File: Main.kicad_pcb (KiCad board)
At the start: 2 copper layers, 99.1 x 78.7 mm, 45 parts, among them J1 Conn_01x01_Female, J10 Conn_01x01_Female, J11 Conn_01x01_Female, J12 Conn_01x01_Female, J2 Conn_01x01_Female, J3 Conn_01x01_Female, J4 Conn_01x02_Female, J5 Conn_01x01_Female, J6 Conn_01x03, J7 Conn_01x03, J8 Conn_01x06, J9 Conn_01x01_Female, Q1 CSD17307Q5A, Q2 CSD17307Q5A, SW1 SW_Push, SW2 SW_Push, SW3 SW_Push, SW4 SW_Push, U1 LTC4002ES8-4.2, U2 SI6423, U3 LTC6995-1, U4 TPS2557

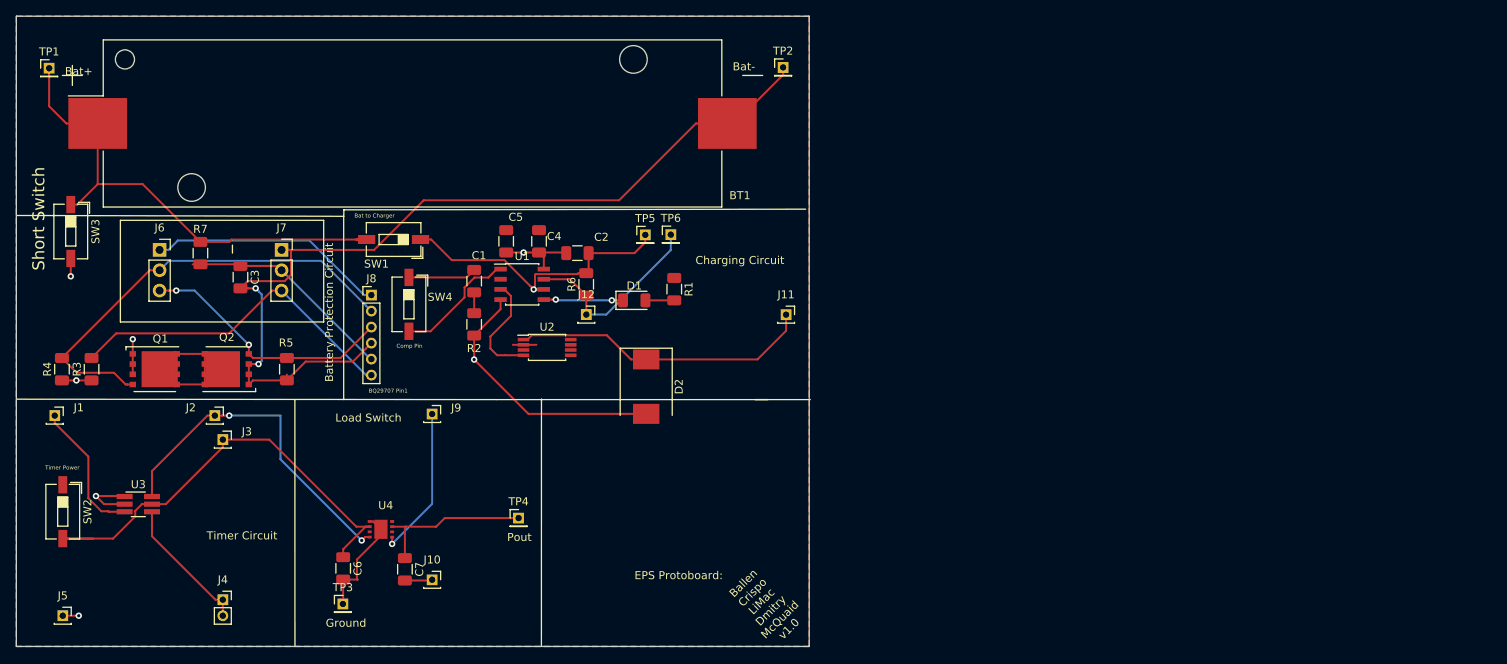
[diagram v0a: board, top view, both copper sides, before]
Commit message: changed_resistor
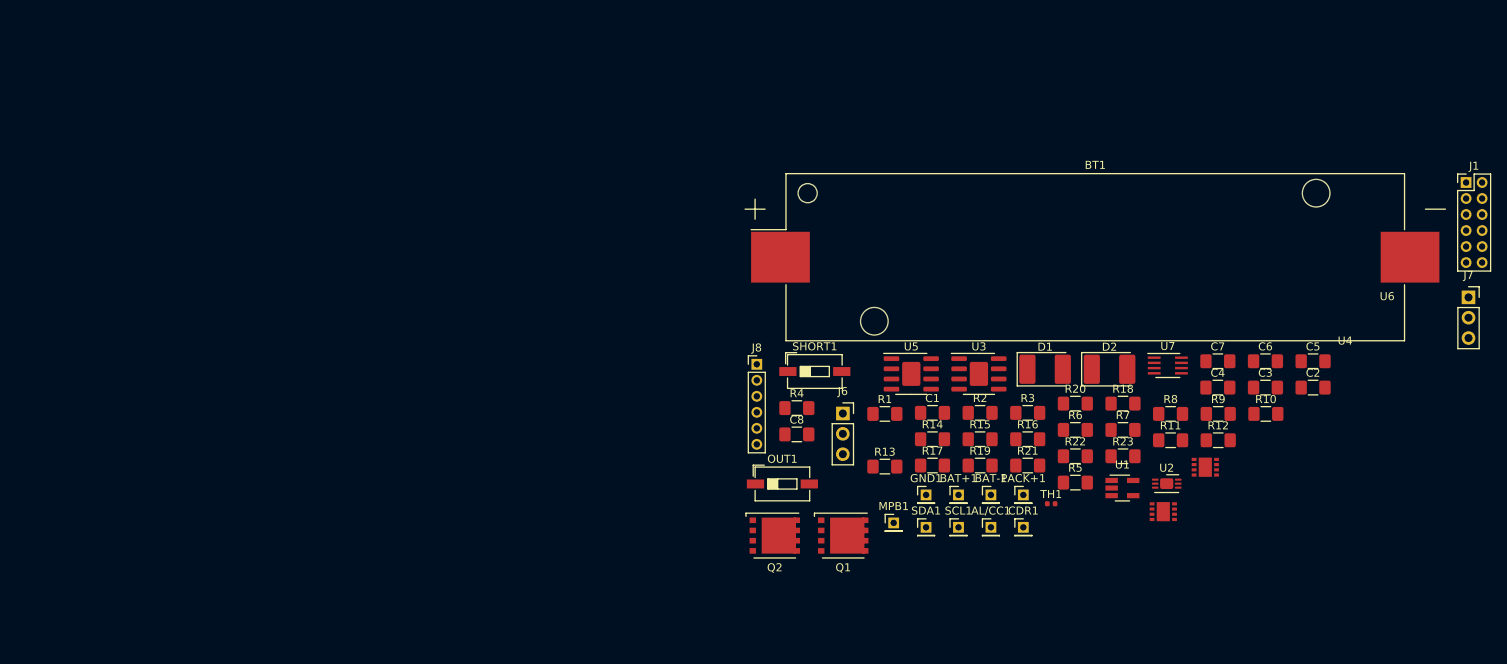
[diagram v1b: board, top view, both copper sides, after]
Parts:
- removed J10, J11, J12, J2, J3, J5, J9: Conn_01x01_Female, Connector_PinSocket_2.00mm:PinSocket_1x01_P2.00mm_Vertical
- removed J4: Conn_01x02_Female, Connector_PinSocket_2.00mm:PinSocket_1x02_P2.00mm_Vertical
- removed SW1, SW2, SW3, SW4: SW_Push, Button_Switch_SMD:SW_DIP_SPSTx01_Slide_6.7x4.1mm_W6.73mm_P2.54mm_LowProfile_JPin
- removed TP1, TP2, TP3, TP4, TP5, TP6: TestPoint, Connector_PinHeader_2.00mm:PinHeader_1x01_P2.00mm_Vertical
- added AL/CC1: TestPoint, Connector_PinHeader_2.00mm:PinHeader_1x01_P2.00mm_Vertical, F.Cu at (145.6, 86.8)
- added BAT+1: TestPoint, Connector_PinHeader_2.00mm:PinHeader_1x01_P2.00mm_Vertical, F.Cu at (141.5, 82.7)
- added BAT-1: TestPoint, Connector_PinHeader_2.00mm:PinHeader_1x01_P2.00mm_Vertical, F.Cu at (145.6, 82.7)
- added C8: 0.1u, Capacitor_SMD:C_1206_3216Metric_Pad1.42x1.75mm_HandSolder, F.Cu at (121.3, 75.2)
- added CDR1: TestPoint, Connector_PinHeader_2.00mm:PinHeader_1x01_P2.00mm_Vertical, F.Cu at (149.6, 86.8)
- added GND1: TestPoint, Connector_PinHeader_2.00mm:PinHeader_1x01_P2.00mm_Vertical, F.Cu at (137.5, 82.7)
- added MPB1: TestPoint, Connector_PinHeader_2.00mm:PinHeader_1x01_P2.00mm_Vertical, F.Cu at (133.4, 86.2)
- added OUT1: SW_Push, Button_Switch_SMD:SW_DIP_SPSTx01_Slide_6.7x4.1mm_W6.73mm_P2.54mm_LowProfile_JPin, F.Cu at (119.5, 81.3)
- added PACK+1: TestPoint, Connector_PinHeader_2.00mm:PinHeader_1x01_P2.00mm_Vertical, F.Cu at (149.6, 82.7)
- added R10: 332k, Resistor_SMD:R_1206_3216Metric_Pad1.42x1.75mm_HandSolder, F.Cu at (179.9, 72.6)
- added R11: 167k, Resistor_SMD:R_1206_3216Metric_Pad1.42x1.75mm_HandSolder, F.Cu at (168.0, 75.9)
- added R12: 1.64M, Resistor_SMD:R_1206_3216Metric_Pad1.42x1.75mm_HandSolder, F.Cu at (174.0, 75.9)
- added R13: 374k, Resistor_SMD:R_1206_3216Metric_Pad1.42x1.75mm_HandSolder, F.Cu at (132.3, 79.2)
- added R14: 1.43M, Resistor_SMD:R_1206_3216Metric_Pad1.42x1.75mm_HandSolder, F.Cu at (138.3, 75.8)
- added R15: 562k, Resistor_SMD:R_1206_3216Metric_Pad1.42x1.75mm_HandSolder, F.Cu at (144.2, 75.8)
- added R16: 14.7m, Resistor_SMD:R_1206_3216Metric_Pad1.42x1.75mm_HandSolder, F.Cu at (150.2, 75.8)
- added R17: 56.2k, Resistor_SMD:R_1206_3216Metric_Pad1.42x1.75mm_HandSolder, F.Cu at (138.3, 79.0)
- added R18: 100k, Resistor_SMD:R_1206_3216Metric_Pad1.42x1.75mm_HandSolder, F.Cu at (162.1, 71.3)
- added R19: 66.5k, Resistor_SMD:R_1206_3216Metric_Pad1.42x1.75mm_HandSolder, F.Cu at (144.2, 79.0)
- added R20: 29.4k, Resistor_SMD:R_1206_3216Metric_Pad1.42x1.75mm_HandSolder, F.Cu at (156.1, 71.3)
- added R21: 59.0k, Resistor_SMD:R_1206_3216Metric_Pad1.42x1.75mm_HandSolder, F.Cu at (150.2, 79.0)
- added R22: 66.5k, Resistor_SMD:R_1206_3216Metric_Pad1.42x1.75mm_HandSolder, F.Cu at (156.1, 77.9)
- added R23: 100k, Resistor_SMD:R_1206_3216Metric_Pad1.42x1.75mm_HandSolder, F.Cu at (162.1, 77.9)
- added R8: 898k, Resistor_SMD:R_1206_3216Metric_Pad1.42x1.75mm_HandSolder, F.Cu at (168.0, 72.6)
- added R9: 28k, Resistor_SMD:R_1206_3216Metric_Pad1.42x1.75mm_HandSolder, F.Cu at (174.0, 72.6)
- added SCL1: TestPoint, Connector_PinHeader_2.00mm:PinHeader_1x01_P2.00mm_Vertical, F.Cu at (141.5, 86.8)
- added SDA1: TestPoint, Connector_PinHeader_2.00mm:PinHeader_1x01_P2.00mm_Vertical, F.Cu at (137.5, 86.8)
- added SHORT1: SW_Push, Button_Switch_SMD:SW_DIP_SPSTx01_Slide_6.7x4.1mm_W6.73mm_P2.54mm_LowProfile_JPin, F.Cu at (123.6, 67.3)
- added TH1: TDK10k, Resistor_SMD:R_0402_1005Metric, F.Cu at (153.1, 83.8)
- added U5: LM393, Package_SO:SOIC-8-1EP_3.9x4.9mm_P1.27mm_EP2.29x3mm, F.Cu at (135.6, 67.6)
- added U6: TPS2557, tps2557:TPS2557, F.Cu at (171.0, 78.3)
- added U7: SN74LVC2G08, Package_SO:SSOP-8_2.95x2.8mm_P0.65mm, F.Cu at (167.7, 66.5)
- C1: value 0.47u -> 0.022uF; footprint Capacitor_SMD:C_1206_3216Metric -> Capacitor_SMD:C_1206_3216Metric_Pad1.42x1.75mm_HandSolder
- C2: value 22u -> 0.1u; footprint Capacitor_SMD:C_1206_3216Metric -> Capacitor_SMD:C_1206_3216Metric_Pad1.42x1.75mm_HandSolder
- C3: footprint Capacitor_SMD:C_1206_3216Metric -> Capacitor_SMD:C_1206_3216Metric_Pad1.42x1.75mm_HandSolder
- C4: value 10u -> 0.1u; footprint Capacitor_SMD:C_1206_3216Metric -> Capacitor_SMD:C_1206_3216Metric_Pad1.42x1.75mm_HandSolder
- C5: value 0.1u -> 0.22u; footprint Capacitor_SMD:C_1206_3216Metric -> Capacitor_SMD:C_1206_3216Metric_Pad1.42x1.75mm_HandSolder
- C6: value 0.1u -> 10u; footprint Capacitor_SMD:C_1206_3216Metric -> Capacitor_SMD:C_1206_3216Metric_Pad1.42x1.75mm_HandSolder
- C7: value 150u -> 0.22u; footprint Capacitor_SMD:C_1206_3216Metric -> Capacitor_SMD:C_1206_3216Metric_Pad1.42x1.75mm_HandSolder
- D1: value LED -> D_Schottky; footprint LED_SMD:LED_1206_3216Metric -> Diode_SMD:D_2114_3652Metric_Castellated
- D2: value B330 -> D_Schottky; footprint Diode_SMD:D_SMC -> Diode_SMD:D_2114_3652Metric_Castellated
- J1: value Conn_01x01_Female -> Conn_02x06_Top_Bottom; footprint Connector_PinSocket_2.00mm:PinSocket_1x01_P2.00mm_Vertical -> Connector_PinHeader_2.00mm:PinHeader_2x06_P2.00mm_Vertical
- R1: value 2k -> 898k; footprint Resistor_SMD:R_1206_3216Metric -> Resistor_SMD:R_1206_3216Metric_Pad1.42x1.75mm_HandSolder
- R2: value 2.2k -> 898k; footprint Resistor_SMD:R_1206_3216Metric -> Resistor_SMD:R_1206_3216Metric_Pad1.42x1.75mm_HandSolder
- R3, R4, R5, R7: footprint Resistor_SMD:R_1206_3216Metric -> Resistor_SMD:R_1206_3216Metric_Pad1.42x1.75mm_HandSolder
- R6: value 59m -> 6k; footprint Resistor_SMD:R_1206_3216Metric -> Resistor_SMD:R_1206_3216Metric_Pad1.42x1.75mm_HandSolder
- U1: value LTC4002ES8-4.2 -> LM4120-CustomSymbols; footprint Package_SO:SOIC-8_3.9x4.9mm_P1.27mm -> Package_TO_SOT_SMD:SOT-23-5_HandSoldering
- U2: value SI6423 -> LTC2942; footprint Package_SO:TSSOP-8_4.4x3mm_P0.65mm -> Package_DFN_QFN:DFN-6-1EP_3x2mm_P0.5mm_EP1.65x1.35mm
- U3: value LTC6995-1 -> LM393; footprint Package_TO_SOT_SMD:TSOT-23-6_HandSoldering -> Package_SO:SOIC-8-1EP_3.9x4.9mm_P1.27mm_EP2.29x3mm
- moved J1 178.7 mm to (205.0, 43.7)
- moved J7 148.4 mm to (205.3, 58.0)
- moved C3 128.8 mm to (179.9, 69.3), turned to 0 degrees
- moved C6 118.1 mm to (179.9, 66.0), turned to 0 degrees
- moved R7 117.4 mm to (162.1, 74.6), turned to 0 degrees
- moved R3 117.1 mm to (150.2, 72.5), turned to 0 degrees
- moved U3 106.3 mm to (144.1, 67.6)
- moved C7 104.8 mm to (173.9, 66.0), turned to 0 degrees
- moved C5 101.9 mm to (185.8, 66.0), turned to 0 degrees
- moved R5 99.5 mm to (156.1, 81.2), turned to 0 degrees
- moved U4 97.8 mm to (165.7, 83.8)
- moved C2 93.4 mm to (185.8, 69.3), turned to 0 degrees
- moved R4 91.9 mm to (121.3, 71.9), turned to 0 degrees
- moved Q1 88.5 mm to (127.1, 87.8)
- moved J6 87.8 mm to (127.1, 72.5)
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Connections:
- BT1 pad 1: BAT -> Net-(BAT+1-Pad1)
- C1 pad 1: Net-(C1-Pad1) -> 5Vref
- C1 pad 2: Net-(C1-Pad2) -> GNDD
- C2 pad 1: Net-(C2-Pad1) -> Net-(BAT+1-Pad1)
- C4 pad 1: +5V -> PACK+
- C5 pad 1: +5V -> Net-(C5-Pad1)
- D1 pad 1: Net-(D1-Pad1) -> PACK+
- D1 pad 2: Net-(D1-Pad2) -> Net-(C6-Pad1)
- D2 pad 1: Net-(D2-Pad1) -> MPB
- D2 pad 2: GNDD -> Net-(C6-Pad1)
- J1 pad 1: Net-(J1-Pad1) -> 5Vref
- R1 pad 1: +5V -> 5Vref
- R1 pad 2: Net-(D1-Pad2) -> BatTemp
- R2 pad 1: Net-(C1-Pad2) -> 5Vref
- R2 pad 2: GNDD -> HighTemp
- R6 pad 1: Net-(J12-Pad1) -> HighTemp
- R6 pad 2: Net-(C2-Pad1) -> GNDA
- R7 pad 1: BAT -> Net-(BAT+1-Pad1)
- U1 pad 2: +5V -> GNDD
- U1 pad 3: Net-(U1-Pad3) -> PACK+
- U1 pad 4: GNDD -> PACK+
- U1 pad 5: Net-(D1-Pad1) -> 5Vref
- U2 pad 1: Net-(D2-Pad1) -> Net-(BAT+1-Pad1)
- U2 pad 2: +5V -> GNDD
- U2 pad 4: Net-(U1-Pad3) -> Net-(SDA1-Pad1)
- U2 pad 7: Net-(U2-Pad7) -> (no net)
- U3 pad 1: GNDD -> TempOK
- U3 pad 2: GNDD -> BatTemp
- U3 pad 3: Net-(J1-Pad1) -> HighTemp
- U3 pad 4: Net-(J4-Pad1) -> GNDA
- U3 pad 5: Net-(C6-Pad1) -> BatTemp
- U3 pad 6: Net-(J2-Pad1) -> LowTemp
- U4 pad 2: Net-(C6-Pad1) -> PACK+
- U4 pad 3: Net-(U4-Pad3) -> PACK+
- U4 pad 4: Net-(J2-Pad1) -> Net-(C5-Pad1)
- U4 pad 6: Net-(U4-Pad6) -> Net-(C6-Pad1)
- U4 pad 7: Net-(C7-Pad1) -> Net-(C6-Pad1)
- U4 pad 8: Net-(U4-Pad8) -> Net-(C5-Pad1)
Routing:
- net /BQ29707_P4: track 117.7 -> 0.00 mm, vias 2 -> 0
- net GNDD: track 80.8 -> 0.00 mm, vias 7 -> 0
- net BAT: track 61.8 -> 0.00 mm
- net Net-(C6-Pad1): track 58.2 -> 0.00 mm
- net /BQ29707_P2: track 56.5 -> 0.00 mm
- net Net-(J2-Pad1): track 43.1 -> 0.00 mm, vias 2 -> 0
- net /BQ29707_P6: track 42.8 -> 0.00 mm
- net Net-(C2-Pad1): track 39.1 -> 0.00 mm, vias 1 -> 0
- net Net-(D2-Pad1): track 37.8 -> 0.00 mm
- net /BQ29707_P3: track 32.2 -> 0.00 mm, vias 2 -> 0
- net /BQ29707_P1: track 29.8 -> 0.00 mm
- net /BQ29707_P5: track 27.2 -> 0.00 mm
- net Net-(J12-Pad1): track 24.3 -> 0.00 mm
- net Net-(C7-Pad1): track 20.2 -> 0.00 mm
- net Net-(Q1-Pad5): track 20.2 -> 0.00 mm
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- removed copper zone on F.Cu, net +5V
- removed copper zone on B.Cu, net GNDD
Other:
- board outline removed
- board text removed: "BQ29707 Pin1"
- board text removed: "Ballen Crispo LiMac Dmitry McQuaid v1.0"
- board text removed: "Bat to Charger"
- board text removed: "Bat+"
- board text removed: "Bat-"
- board text removed: "Battery Protection Circuit"
- board text removed: "Charging Circuit"
- board text removed: "Comp Pin"
- board text removed: "EPS Protoboard:"
- board text removed: "Ground"
- board text removed: "Load Switch"
- board text removed: "Pout"
- board text removed: "Short Switch"
- board text removed: "Timer Circuit"
- board text removed: "Timer Power"
